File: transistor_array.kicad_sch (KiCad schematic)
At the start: 4 parts, among them Q14 MMBT3904_C181119, Q33 MMBT3904_C181119, Q34 MMBT3904_C181119, Q35 MMBT3904_C181119

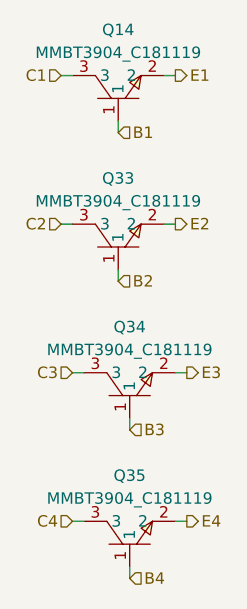
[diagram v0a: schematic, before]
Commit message: Board malfunction fixes
- Changed F1-F4, R5, R6 to 3V (previous 5V caused failure).

- Connected STM32DISC1 to 5V and 3V outputs/inputs

- Moved SDA to PC9 (was PA9) and ENC3_A to PC6 (was PC3).

- Redesigned MPU6050 layout to resolve stability and connectivity issues.

- Isolated PCA6587 buzzer with a transistor.
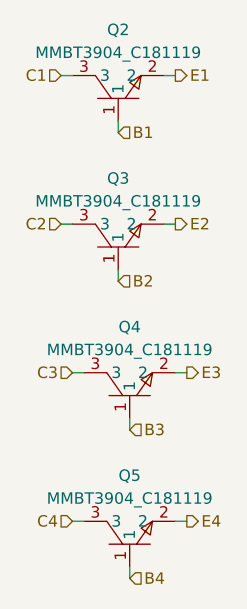
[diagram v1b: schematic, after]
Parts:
- renumbered Q14 to Q2, Q33 to Q3, Q34 to Q4, Q35 to Q5
